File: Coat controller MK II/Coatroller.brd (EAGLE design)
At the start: 58.4 x 21.6 mm, 11 parts, among them U1 ATMEGA328P_PDIP, U2 V_REG_LDOSMD, Y1 ABM3B-16.000MHZ-B2-T

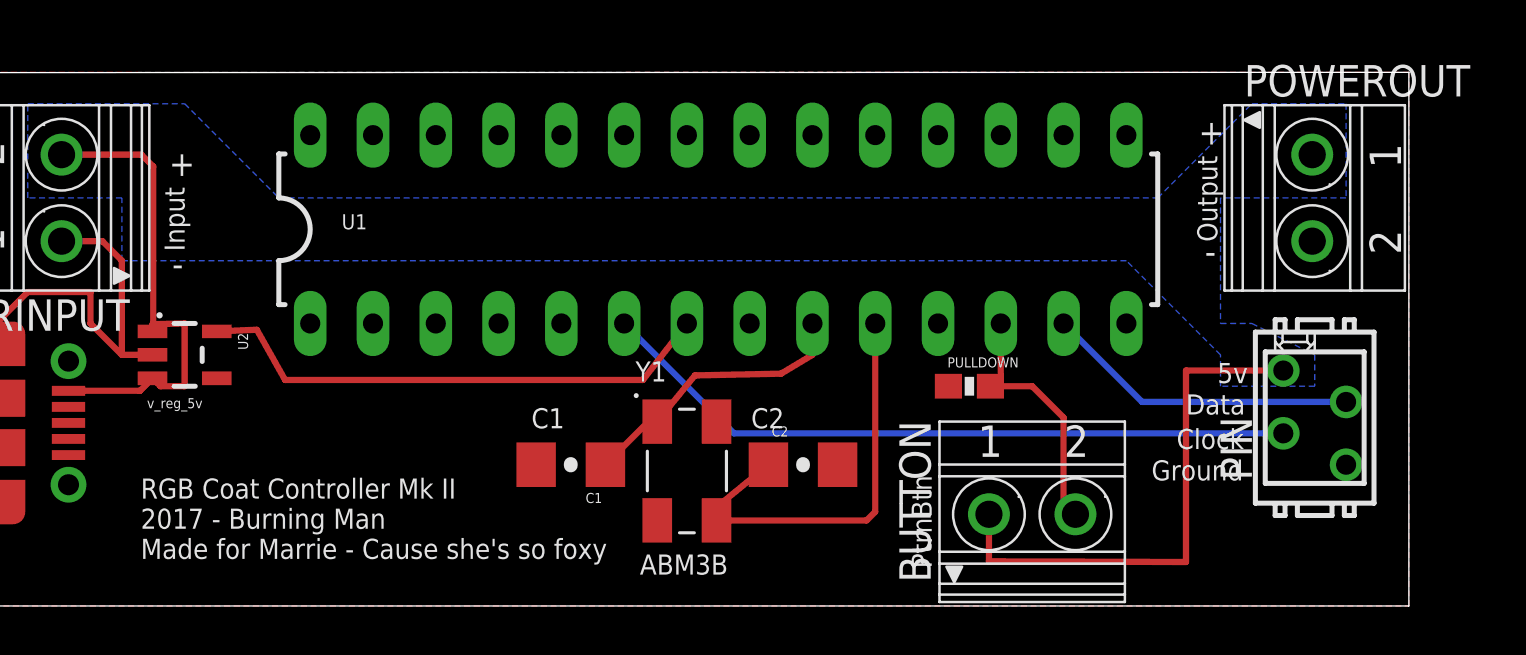
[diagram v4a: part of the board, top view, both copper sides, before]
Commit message: rotated micromatch to proper direction and rerouted. Fixed a few crossed routes
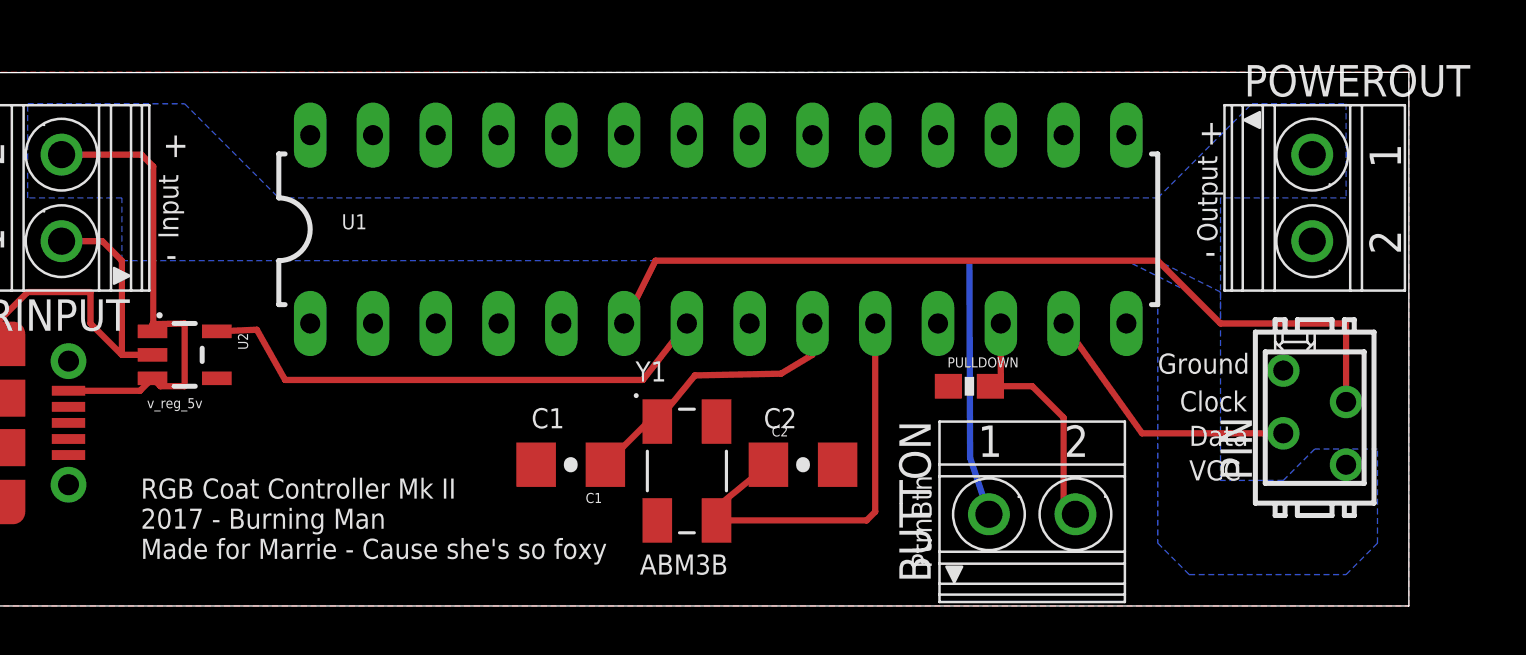
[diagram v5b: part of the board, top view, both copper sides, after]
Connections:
- net CLOCK: now also PIN.2; no longer PIN.3
- net DATA: now also PIN.3; no longer PIN.2
- net GROUND: now also PIN.1; no longer PIN.4
- net VCC: now also PIN.4; no longer PIN.1
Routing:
- net VCC: track 41.4 -> 30.2 mm
- net CLOCK: track 28.5 -> 35.0 mm
- net DATA: track 12.7 -> 11.2 mm
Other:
- board text added: "VCC"
- board text removed: "5v"
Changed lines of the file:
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@@
 <wire x1="0" y1="21.58" x2="0" y2="0" width="0" layer="20"/>
 <text x="7.366" y="8.001" size="0.4064" layer="21" ratio="15">v_reg_5v</text>
-<text x="8.255" y="17.399" size="1.016" layer="21" ratio="15">+</text>
-<text x="8.382" y="13.335" size="1.016" layer="21" ratio="15">-</text>
+<text x="8.001" y="18.161" size="1.016" layer="21" ratio="15">+</text>
+<text x="8.128" y="13.716" size="1.016" layer="21" ratio="15">-</text>
 <text x="50.165" y="13.843" size="1.016" layer="21" ratio="15">-</text>
 <text x="49.911" y="18.669" size="1.016" layer="21" ratio="15">+</text>
 <text x="50.673" y="14.732" size="0.8128" layer="21" ratio="15" rot="R90">Output</text>
-<text x="50.673" y="9.017" size="0.8128" layer="21" ratio="15">5v</text>
-<text x="49.403" y="7.747" size="0.8128" layer="21" ratio="15">Data</text>
-<text x="49.022" y="6.35" size="0.8128" layer="21" ratio="15">Clock</text>
-<text x="48.006" y="5.08" size="0.8128" layer="21" ratio="15">Ground</text>
+<text x="49.53" y="5.08" size="0.8128" layer="21" ratio="15">VCC</text>
+<text x="49.53" y="6.477" size="0.8128" layer="21" ratio="15">Data</text>
+<text x="49.149" y="7.874" size="0.8128" layer="21" ratio="15">Clock</text>
+<text x="48.26" y="9.398" size="0.8128" layer="21" ratio="15">Ground</text>
 <text x="27.305" y="1.27" size="0.8128" layer="21" ratio="15">ABM3B</text>
 <text x="24.257" y="8.001" size="0.8128" layer="21" ratio="15" rot="R180">C1</text>
-<text x="8.89" y="14.351" size="0.8128" layer="21" ratio="15" rot="R90">Input</text>
+<text x="8.636" y="14.859" size="0.8128" layer="21" ratio="15" rot="R90">Input</text>
 <text x="7.112" y="1.905" size="0.8128" layer="21" ratio="15">RGB Coat Controller Mk II
 2017 - Burning Man
@@
 <text x="21.59" y="3.81" size="0.8128" layer="22" ratio="15" rot="MR0">Made by Remington Winters
 </text>
-<text x="33.147" y="8.001" size="0.8128" layer="21" ratio="15" rot="R180">C2</text>
+<text x="33.655" y="8.001" size="0.8128" layer="21" ratio="15" rot="R180">C2</text>
 <text x="39.116" y="1.524" size="0.8128" layer="21" font="vector" ratio="15" rot="R90">PtrnBtn</text>
 </plain>
@@
 <signals>
 <signal name="GROUND">
+<polygon width="0.254" layer="1">
+<vertex x="0" y="21.59"/>
+<vertex x="0" y="0"/>
+<vertex x="58.42" y="0"/>
+<vertex x="58.42" y="21.59"/>
+</polygon>
 <contactref element="POWERINPUT" pad="1"/>
 <contactref element="POWEROUT" pad="2"/>
@@
 <contactref element="U$1" pad="5"/>
 <contactref element="U1" pad="8"/>
-<contactref element="PIN" pad="4"/>
+<contactref element="C1" pad="2"/>
+<contactref element="C2" pad="2"/>
+<contactref element="Y1" pad="2"/>
+<contactref element="Y1" pad="4"/>
+<contactref element="PULLDOWN" pad="1"/>
 <wire x1="1.27" y1="11.43" x2="2.54" y2="12.7" width="0.254" layer="1"/>
 <wire x1="2.54" y1="12.7" x2="5.08" y2="12.7" width="0.254" layer="1"/>
@@
 <wire x1="5.56" y1="14.76" x2="6.35" y2="13.97" width="0.254" layer="1"/>
 <wire x1="6.35" y1="13.97" x2="6.35" y2="10.16" width="0.254" layer="1"/>
-<polygon width="0.254" layer="1">
-<vertex x="0" y="21.59"/>
-<vertex x="0" y="0"/>
-<vertex x="58.42" y="0"/>
-<vertex x="58.42" y="21.59"/>
-</polygon>
-<contactref element="C1" pad="2"/>
-<contactref element="C2" pad="2"/>
-<contactref element="Y1" pad="2"/>
-<contactref element="Y1" pad="4"/>
-<contactref element="PULLDOWN" pad="1"/>
+<contactref element="PIN" pad="1"/>
 </signal>
 <signal name="VCC">
@@
 <contactref element="POWEROUT" pad="1"/>
 <contactref element="U2" pad="1"/>
-<contactref element="PIN" pad="1"/>
 <wire x1="3.91" y1="18.26" x2="7.14" y2="18.26" width="0.254" layer="1"/>
 <wire x1="7.14" y1="18.26" x2="7.62" y2="17.78" width="0.254" layer="1"/>
@@
 <vertex x="50.8" y="16.51"/>
 <vertex x="50.8" y="11.43"/>
-<vertex x="52.07" y="11.43"/>
-<vertex x="54.61" y="10.16"/>
-<vertex x="54.61" y="8.89"/>
-<vertex x="50.8" y="8.89"/>
-<vertex x="50.8" y="10.16"/>
+<vertex x="49.53" y="12.7"/>
 <vertex x="46.99" y="13.97"/>
 <vertex x="6.35" y="13.97"/>
@@
 </polygon>
 <contactref element="BUTTON" pad="1"/>
-<wire x1="41.43" y1="3.71" x2="41.429" y2="1.805" width="0.254" layer="1"/>
-<wire x1="41.429" y1="1.805" x2="49.403" y2="1.778" width="0.254" layer="1"/>
-<wire x1="49.403" y1="1.778" x2="49.403" y2="9.525" width="0.254" layer="1"/>
 <wire x1="4.191" y1="8.706" x2="7.0859" y2="8.706" width="0.254" layer="1"/>
 <wire x1="7.0859" y1="8.706" x2="7.5899" y2="9.21" width="0.254" layer="1"/>
-<wire x1="49.403" y1="9.525" x2="53.34" y2="9.525" width="0.254" layer="1"/>
+<wire x1="41.43" y1="3.71" x2="40.668" y2="5.997" width="0.254" layer="16"/>
+<wire x1="40.668" y1="5.997" x2="40.64" y2="13.97" width="0.254" layer="16"/>
+<contactref element="PIN" pad="4"/>
+<polygon width="0.254" layer="16">
+<vertex x="48.26" y="13.97"/>
+<vertex x="48.26" y="2.54"/>
+<vertex x="49.53" y="1.27"/>
+<vertex x="55.88" y="1.27"/>
+<vertex x="57.15" y="2.54"/>
+<vertex x="57.15" y="6.35"/>
+<vertex x="54.61" y="6.35"/>
+<vertex x="53.34" y="5.08"/>
+<vertex x="50.8" y="5.08"/>
+<vertex x="50.8" y="12.7"/>
+</polygon>
 </signal>
 <signal name="5V">
@@
 <wire x1="36.83" y1="3.81" x2="36.83" y2="11.43" width="0.254" layer="1"/>
 </signal>
-<signal name="DATA">
+<signal name="CLOCK">
+<contactref element="U1" pad="6"/>
 <contactref element="PIN" pad="2"/>
-<contactref element="U1" pad="13"/>
-<wire x1="55.88" y1="8.255" x2="47.625" y2="8.255" width="0.254" layer="16"/>
-<wire x1="47.625" y1="8.255" x2="44.45" y2="11.43" width="0.254" layer="16"/>
-</signal>
-<signal name="CLOCK">
-<contactref element="PIN" pad="3"/>
-<contactref element="U1" pad="6"/>
-<wire x1="53.34" y1="6.985" x2="31.115" y2="6.985" width="0.254" layer="16"/>
-<wire x1="31.115" y1="6.985" x2="26.67" y2="11.43" width="0.254" layer="16"/>
+<wire x1="55.88" y1="8.255" x2="55.88" y2="11.43" width="0.254" layer="1"/>
+<wire x1="55.88" y1="11.43" x2="50.8" y2="11.43" width="0.254" layer="1"/>
+<wire x1="50.8" y1="11.43" x2="48.26" y2="13.97" width="0.254" layer="1"/>
+<wire x1="48.26" y1="13.97" x2="27.94" y2="13.97" width="0.254" layer="1"/>
+<wire x1="27.94" y1="13.97" x2="26.67" y2="11.43" width="0.254" layer="1"/>
 </signal>
 <signal name="BUTTONPIN">
@@
 <wire x1="44.45" y1="4.19" x2="44.93" y2="3.71" width="0.254" layer="1"/>
 </signal>
+<signal name="DATA">
+<contactref element="U1" pad="13"/>
+<contactref element="PIN" pad="3"/>
+<wire x1="53.34" y1="6.985" x2="47.625" y2="6.985" width="0.254" layer="1"/>
+<wire x1="47.625" y1="6.985" x2="44.45" y2="11.43" width="0.254" layer="1"/>
+</signal>
 </signals>

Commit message: expect this is production level
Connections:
- net GROUND: now also U1.22
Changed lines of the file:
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@@
 <layer number="45" name="Holes" color="7" fill="1" visible="yes" active="yes"/>
 <layer number="46" name="Milling" color="3" fill="1" visible="no" active="yes"/>
-<layer number="47" name="Measures" color="7" fill="1" visible="yes" active="yes"/>
-<layer number="48" name="Document" color="7" fill="1" visible="yes" active="yes"/>
-<layer number="49" name="Reference" color="7" fill="1" visible="yes" active="yes"/>
+<layer number="47" name="Measures" color="7" fill="1" visible="no" active="yes"/>
+<layer number="48" name="Document" color="7" fill="1" visible="no" active="yes"/>
+<layer number="49" name="Reference" color="7" fill="1" visible="no" active="yes"/>
 <layer number="50" name="dxf" color="7" fill="1" visible="no" active="no"/>
 <layer number="51" name="tDocu" color="6" fill="1" visible="yes" active="yes"/>
@@
 <text x="49.149" y="7.874" size="0.8128" layer="21" ratio="15">Clock</text>
 <text x="48.26" y="9.398" size="0.8128" layer="21" ratio="15">Ground</text>
-<text x="27.305" y="1.27" size="0.8128" layer="21" ratio="15">ABM3B</text>
+<text x="31.115" y="2.54" size="0.8128" layer="21" ratio="15">ABM3B</text>
 <text x="24.257" y="8.001" size="0.8128" layer="21" ratio="15" rot="R180">C1</text>
 <text x="8.636" y="14.859" size="0.8128" layer="21" ratio="15" rot="R90">Input</text>
-<text x="7.112" y="1.905" size="0.8128" layer="21" ratio="15">RGB Coat Controller Mk II
+<text x="5.461" y="-1.016" size="1.016" layer="21" ratio="15">RGB Coat Controller Mk II
 2017 - Burning Man
 Made for Marrie - Cause she's so foxy
@@
 <wire x1="6.35" y1="13.97" x2="6.35" y2="10.16" width="0.254" layer="1"/>
 <contactref element="PIN" pad="1"/>
+<contactref element="U1" pad="22"/>
 </signal>
 <signal name="VCC">
